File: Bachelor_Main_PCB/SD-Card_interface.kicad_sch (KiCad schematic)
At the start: 1 part, among them J16 F32Q-1A7H1-11022

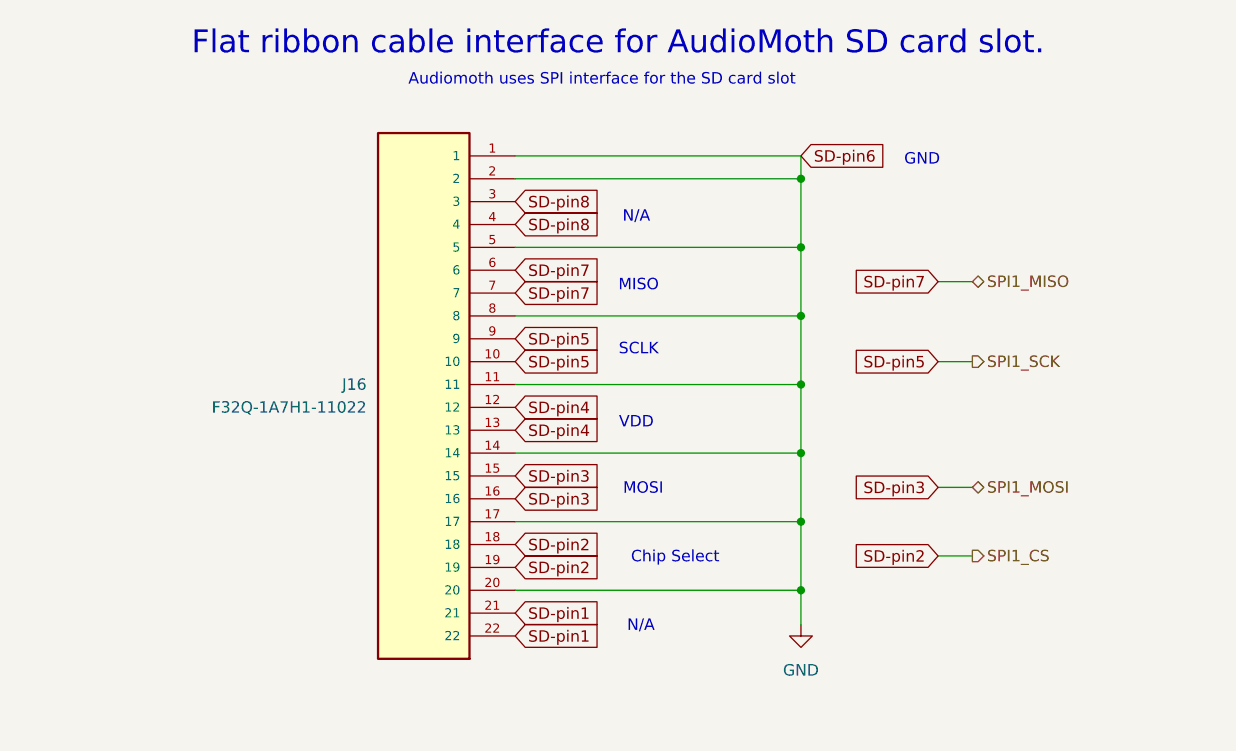
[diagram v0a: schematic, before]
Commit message: Removed Modem_safe_PWR_remove pin.
was potential use for the MCU but would require level shifters and would not add any functionality ass the RPI controls the Modem anyway.
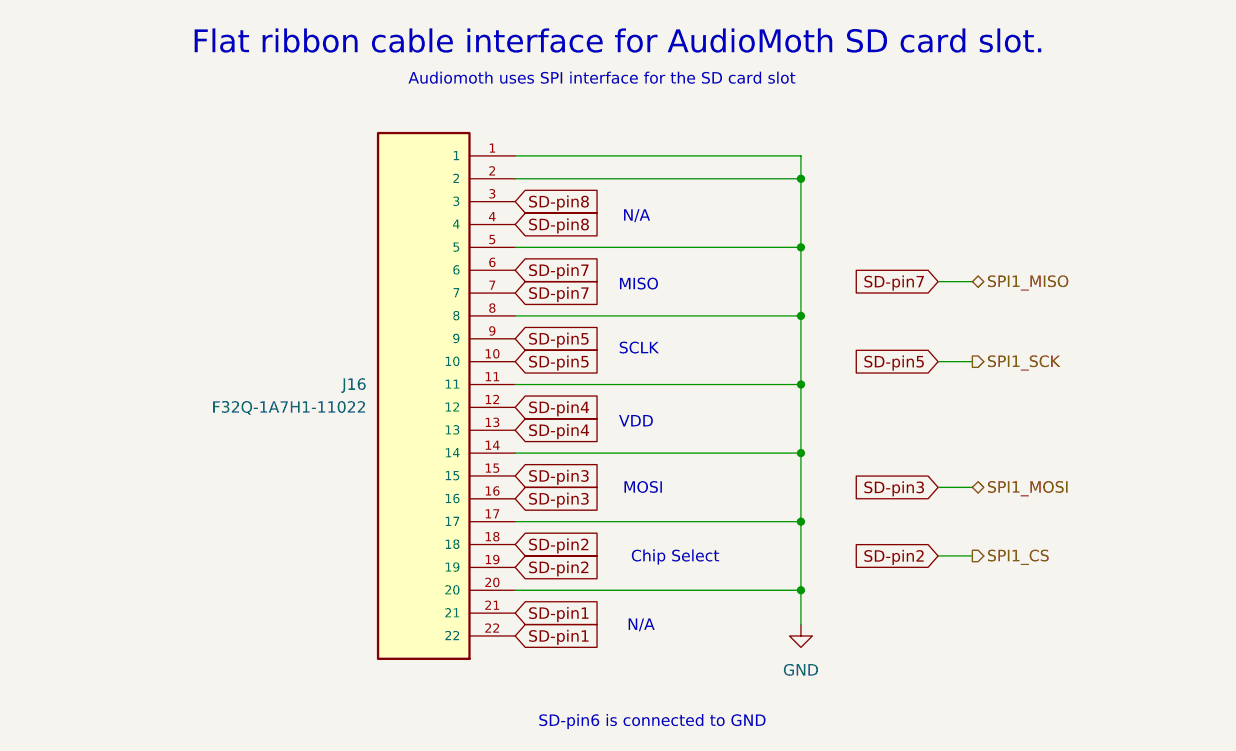
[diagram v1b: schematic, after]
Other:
- note added: "SD-pin6 is connected to GND"
- note removed: "GND"
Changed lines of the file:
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@@
-		)
-	)
-	(text "GND"
-		(exclude_from_sim no)
-		(at 159.512 57.658 0)
-		(effects
-			(font
-				(size 1.27 1.27)
-			)
 		)
 	)
@@
 		)
 	)
+	(text "SD-pin6 is connected to GND"
+		(exclude_from_sim no)
+		(at 129.54 120.142 0)
+		(effects
+			(font
+				(size 1.27 1.27)
+			)
+		)
+	)
 	(junction
 		(at 146.05 82.55)
@@
 				(hide yes)
 			)
-		)
-	)
-	(global_label "SD-pin6"
-		(shape input)
-		(at 146.05 57.15 0)
-		(fields_autoplaced yes)
-		(effects
-			(font
-				(size 1.27 1.27)
-			)
-			(justify left)
-		)
-		(property "Intersheetrefs" "${INTERSHEET_REFS}"
-			(at 157.1994 57.15 0)
-			(effects
-				(font
-					(size 1.27 1.27)
-				)
-				(justify left)
-				(hide yes)
-			)

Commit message: Imported components from schematic to PCB and Reanotat all designators
THis means every designator is now different and the references made prior no longer applies
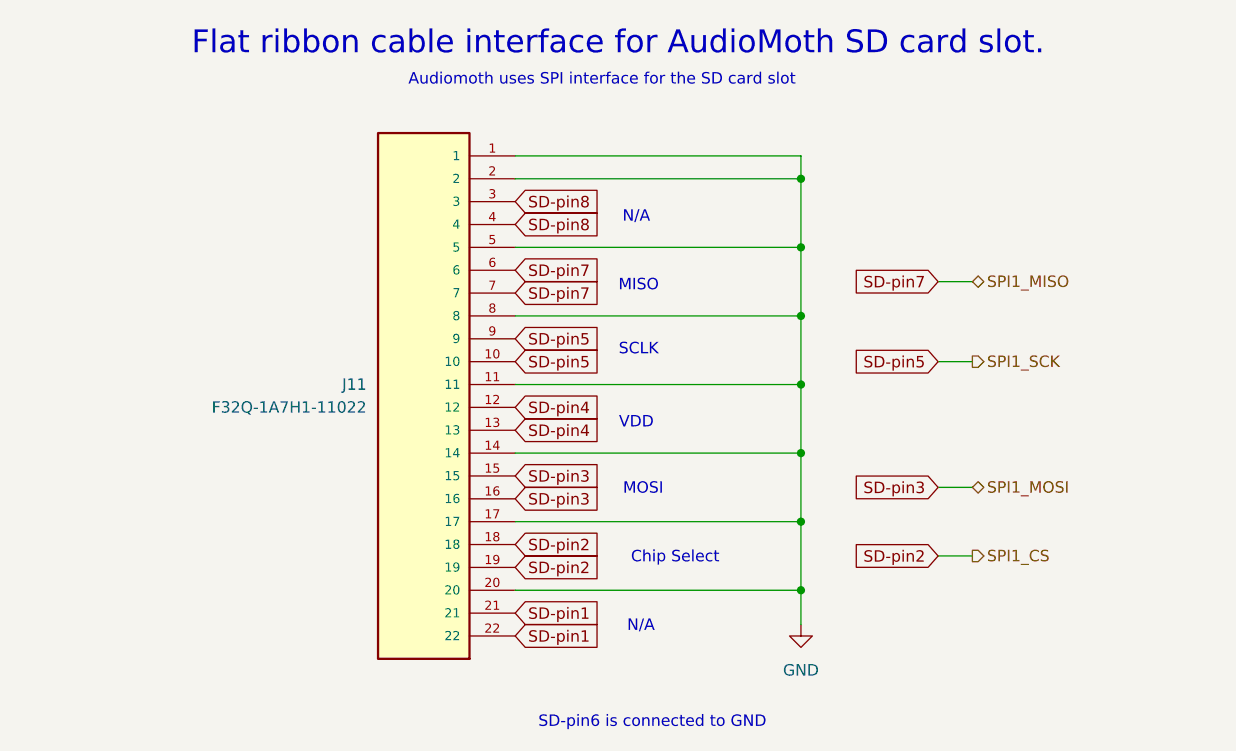
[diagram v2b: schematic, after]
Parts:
- renumbered J16 to J11
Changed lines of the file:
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@@
 		(on_board yes)
 		(dnp no)
-		(property "Reference" "J16"
+		(property "Reference" "J11"
 			(at 97.79 82.5499 0)
 			(effects
@@
 			(project "Bachelor_Main_PCB"
 				(path "/3544d663-329e-4884-b753-28436ca187e8/e2053849-b1b4-4732-a0d8-f90e27301853"
-					(reference "J16")
+					(reference "J11")
 					(unit 1)
 				)
@@
 		(dnp no)
 		(fields_autoplaced yes)
-		(property "Reference" "#PWR02"
+		(property "Reference" "#PWR038"
 			(at 146.05 115.57 0)
 			(effects
@@
 			(project "Bachelor_Main_PCB"
 				(path "/3544d663-329e-4884-b753-28436ca187e8/e2053849-b1b4-4732-a0d8-f90e27301853"
-					(reference "#PWR02")
+					(reference "#PWR038")
 					(unit 1)
 				)
